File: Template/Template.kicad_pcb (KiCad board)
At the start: 2 copper layers, 85 x 100 mm, 19 parts

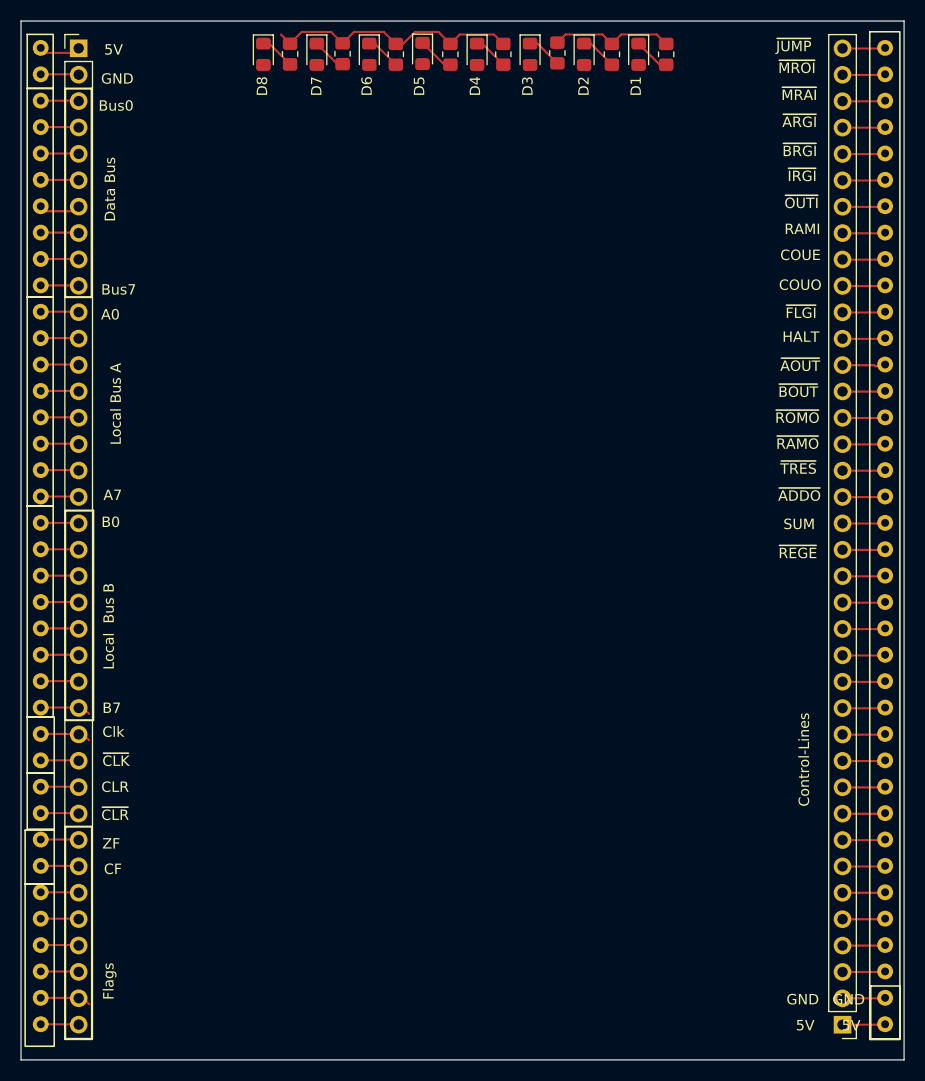
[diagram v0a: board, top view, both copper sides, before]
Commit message: Template PCB size adjustment
Keeping it within the PCBWay $5 size
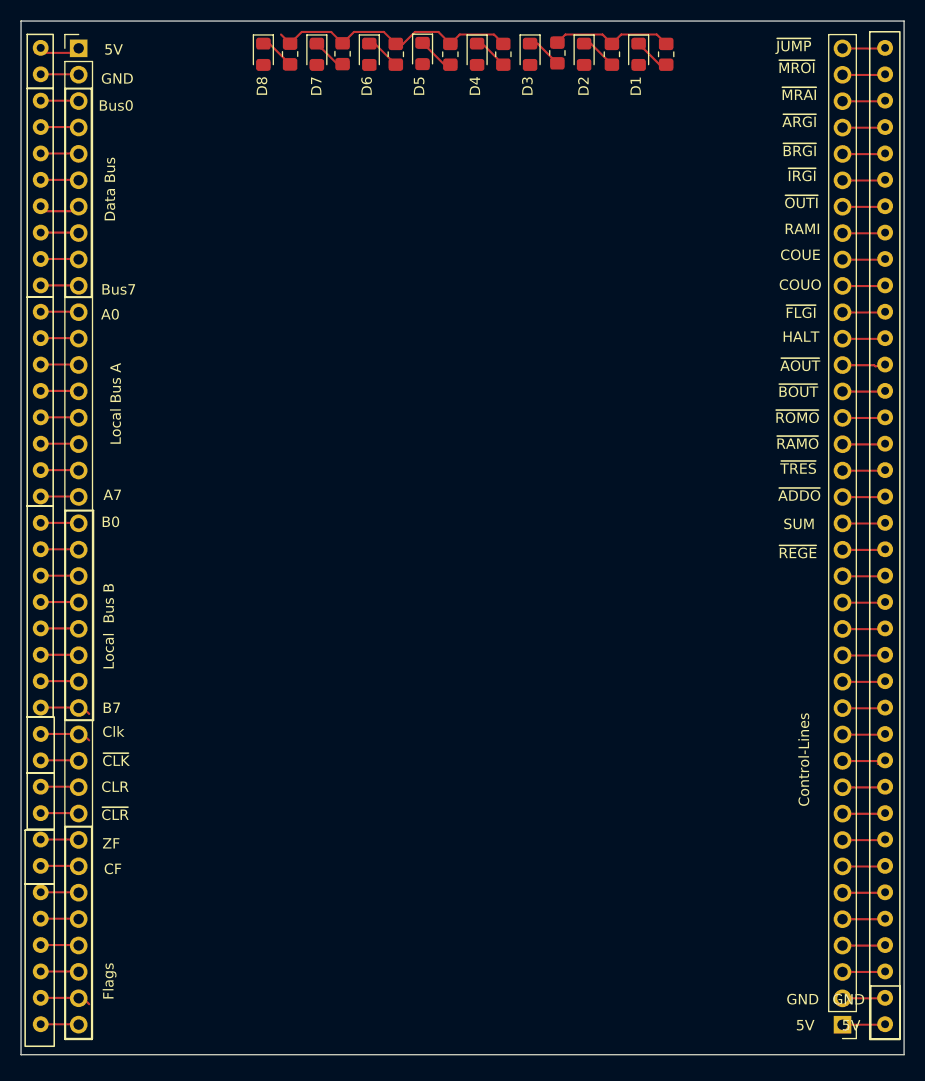
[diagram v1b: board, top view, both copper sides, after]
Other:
- board size 85 x 100 mm -> 85 x 99.5 mm
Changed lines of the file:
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@@
 	(gr_rect
 		(start 23.725 28.675)
-		(end 108.725 128.675)
+		(end 108.725 128.175)
 		(stroke
 			(width 0.05)

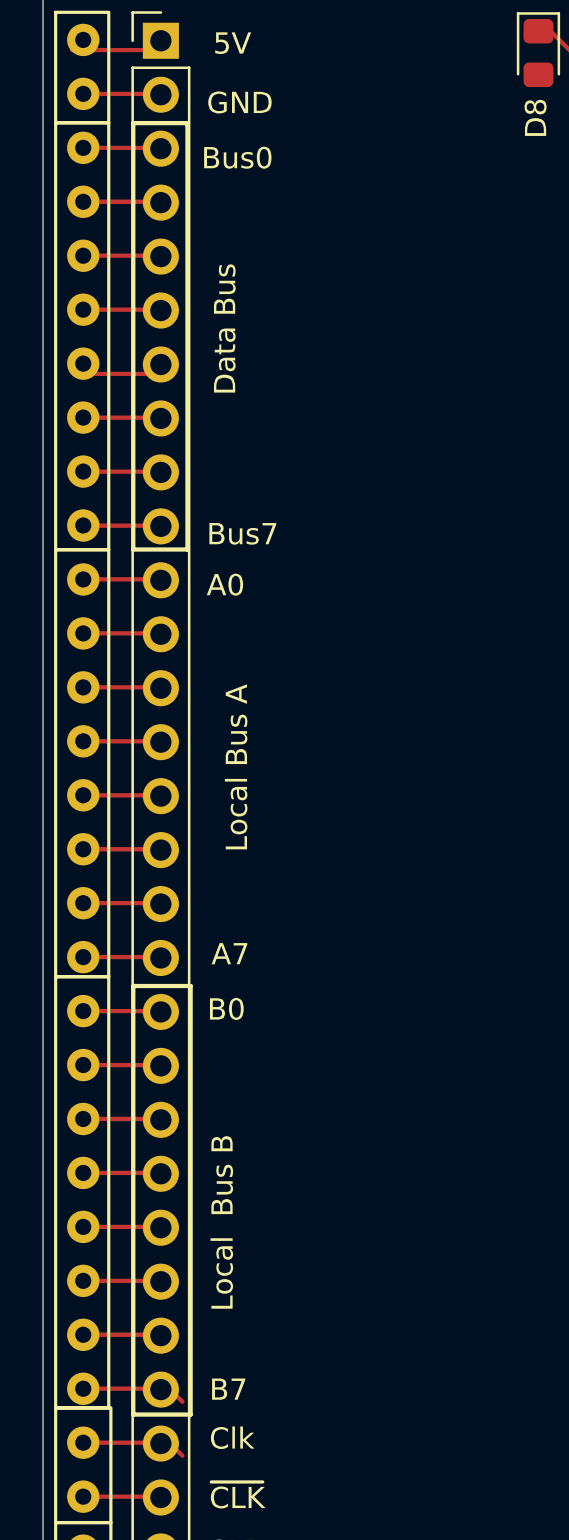
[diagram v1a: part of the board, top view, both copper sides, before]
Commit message: Fixed some issues with the orientation of the local buses on the side-rails.
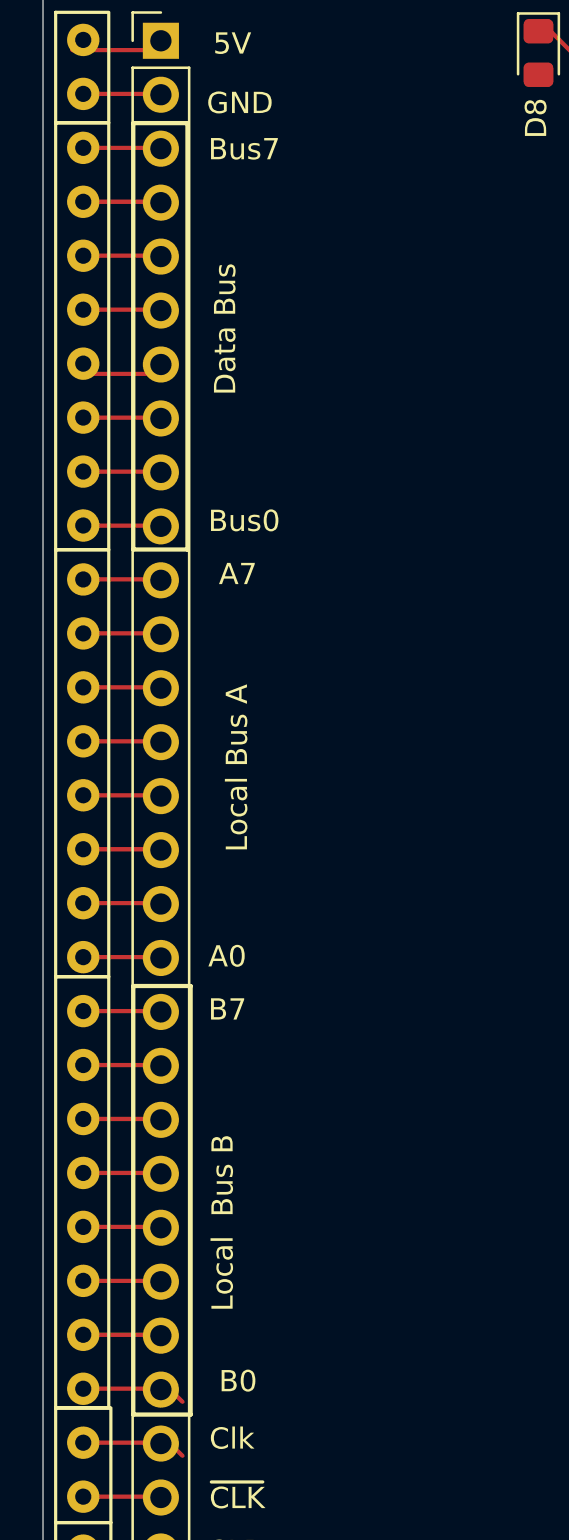
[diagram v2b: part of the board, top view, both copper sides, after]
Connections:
- B2 pad 10: BUS7 -> BUS0
- B2 pad 11: LBA0 -> LBA7
- B2 pad 12: LBA1 -> LBA6
- B2 pad 13: LBA2 -> LBA5
- B2 pad 14: LBA3 -> LBA4
- B2 pad 15: LBA4 -> LBA3
- B2 pad 16: LBA5 -> LBA2
- B2 pad 17: LBA6 -> LBA1
- B2 pad 18: LBA7 -> LBA0
- B2 pad 19: LBB0 -> LBB7
- B2 pad 20: LBB1 -> LBB6
- B2 pad 21: LBB2 -> LBB5
- B2 pad 22: LBB3 -> LBB4
- B2 pad 23: LBB4 -> LBB3
- B2 pad 24: LBB5 -> LBB2
- B2 pad 25: LBB6 -> LBB1
- B2 pad 26: LBB7 -> LBB0

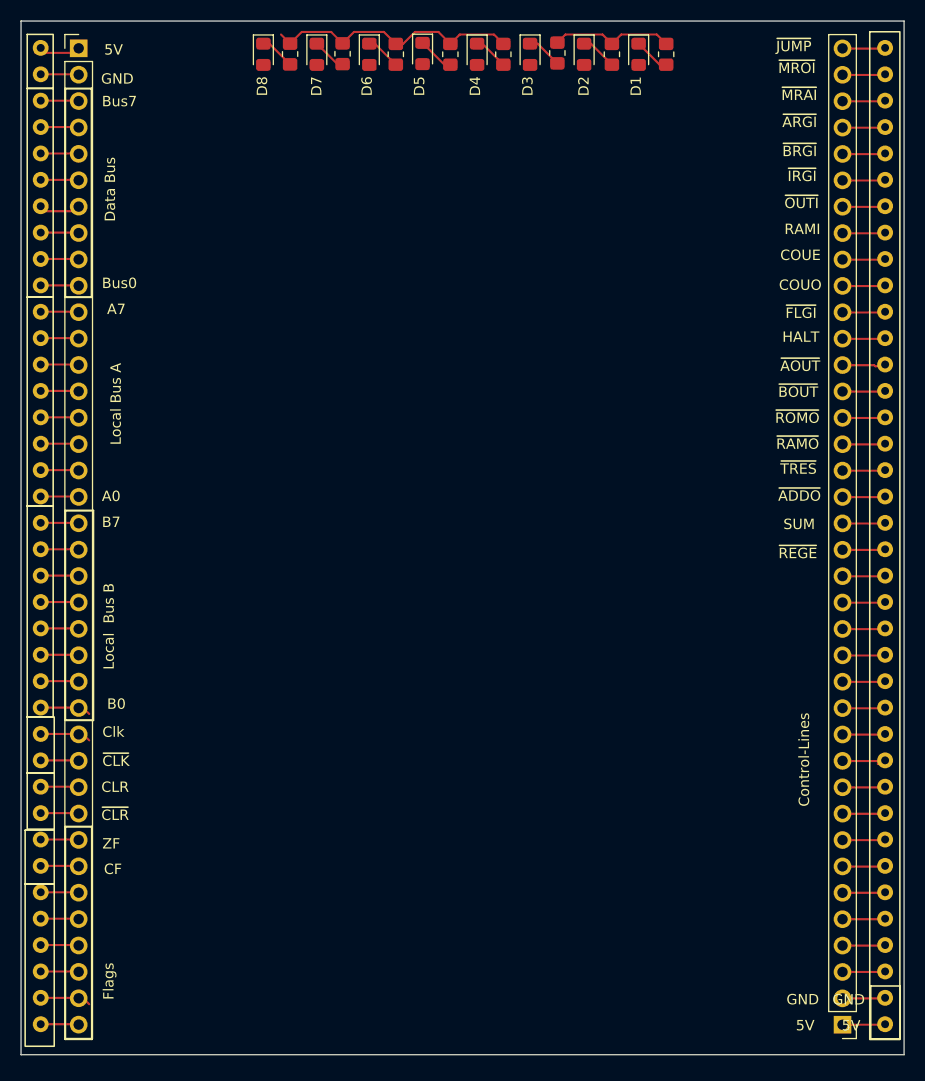
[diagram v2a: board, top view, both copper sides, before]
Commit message: [Template] - fixed the ordering of the buses in the schematic and PCB labels. Bit 0 is now always at the top.
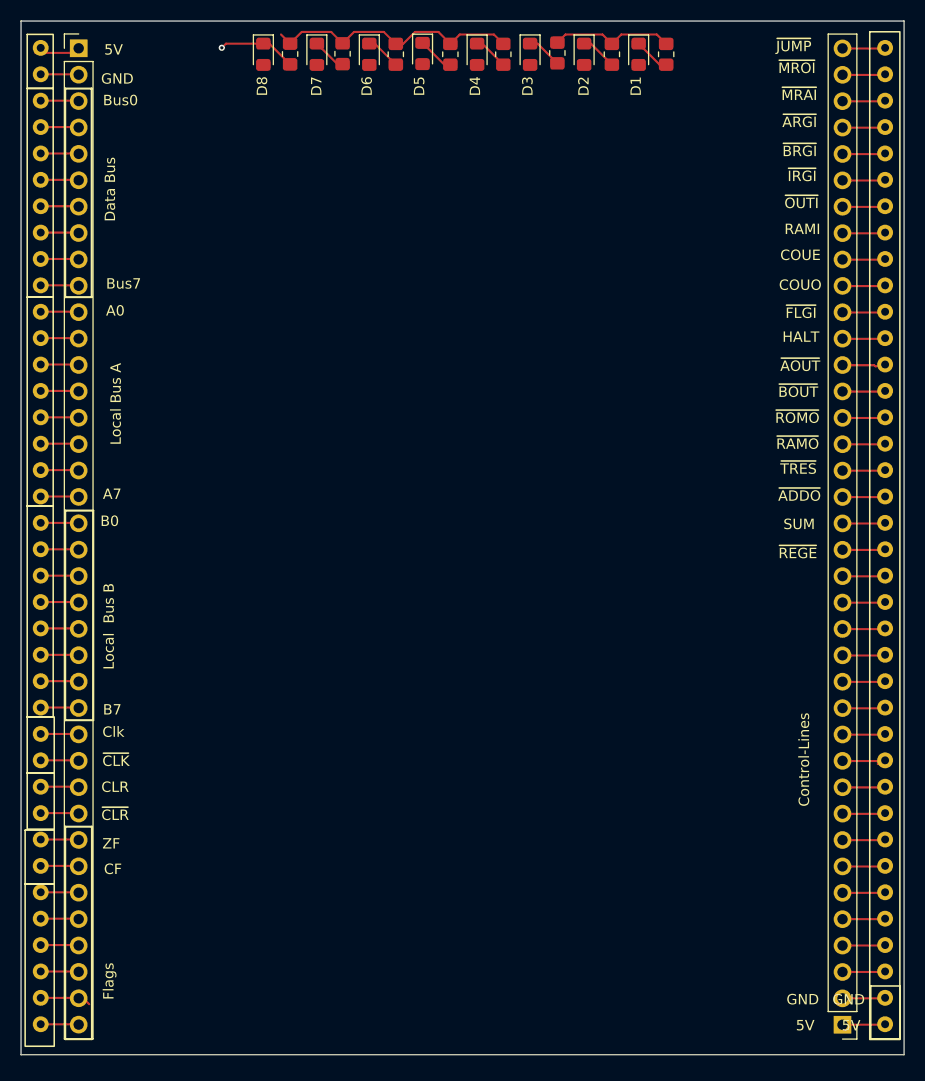
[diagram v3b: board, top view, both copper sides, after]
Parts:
- R1, R2, R3, R4, R5, R6, R7, R8: value 220 Ohm -> 330R
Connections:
- B2 pad 10: BUS0 -> BUS7
- B2 pad 11: LBA7 -> LBA0
- B2 pad 12: LBA6 -> LBA1
- B2 pad 13: LBA5 -> LBA2
- B2 pad 14: LBA4 -> LBA3
- B2 pad 15: LBA3 -> LBA4
- B2 pad 16: LBA2 -> LBA5
- B2 pad 17: LBA1 -> LBA6
- B2 pad 18: LBA0 -> LBA7
- B2 pad 19: LBB7 -> LBB0
- B2 pad 20: LBB6 -> LBB1
- B2 pad 21: LBB5 -> LBB2
- B2 pad 22: LBB4 -> LBB3
- B2 pad 23: LBB3 -> LBB4
- B2 pad 24: LBB2 -> LBB5
- B2 pad 25: LBB1 -> LBB6
- B2 pad 26: LBB0 -> LBB7
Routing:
- net Net-(D8-K): track 3.40 -> 7.57 mm, vias 0 -> 1
